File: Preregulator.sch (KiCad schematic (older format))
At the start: 26 parts, among them Q1 3904, Q2 3904, Q3 4403, Q4 4403, Q5 AO4805

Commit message: First working version
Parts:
- added C48: 100n, IPC7351-Nominal:CAPC1608X55, symbol C-0603
- added C55: 470u, pth-passive:C-ALUM-10mm, symbol C-ALUM-10mm
- added TP5: PREREG, conn-test:TEST-SMD-SMALL, symbol TESTPOINT
- L1: footprint manuf:BOURNS-SRN5040 -> (none); BOM (none) -> DIST DIGIKEY M8921-ND
- R17: value 20k -> 22k; BOM RES SMD 20k 1% [0603] -> RES SMD 22k 1% [0603]
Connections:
- net labels added: GND, PWR
- net labels removed: PWRGND
- wire segments 61 -> 67
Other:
- note added: "-0.5V"
- note added: "0V"
- note added: "3.3V"
- note added: "Vin"
- note added: "Vin-0.7V"
- note added: "Vin-13.9V"
- note added: "Vin-14.6V"
- note removed: "M8921-ND"
- moved on the sheet: C1, C2, C24, C25, C26, C3, C4, C41, C5, C6, D1, L1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

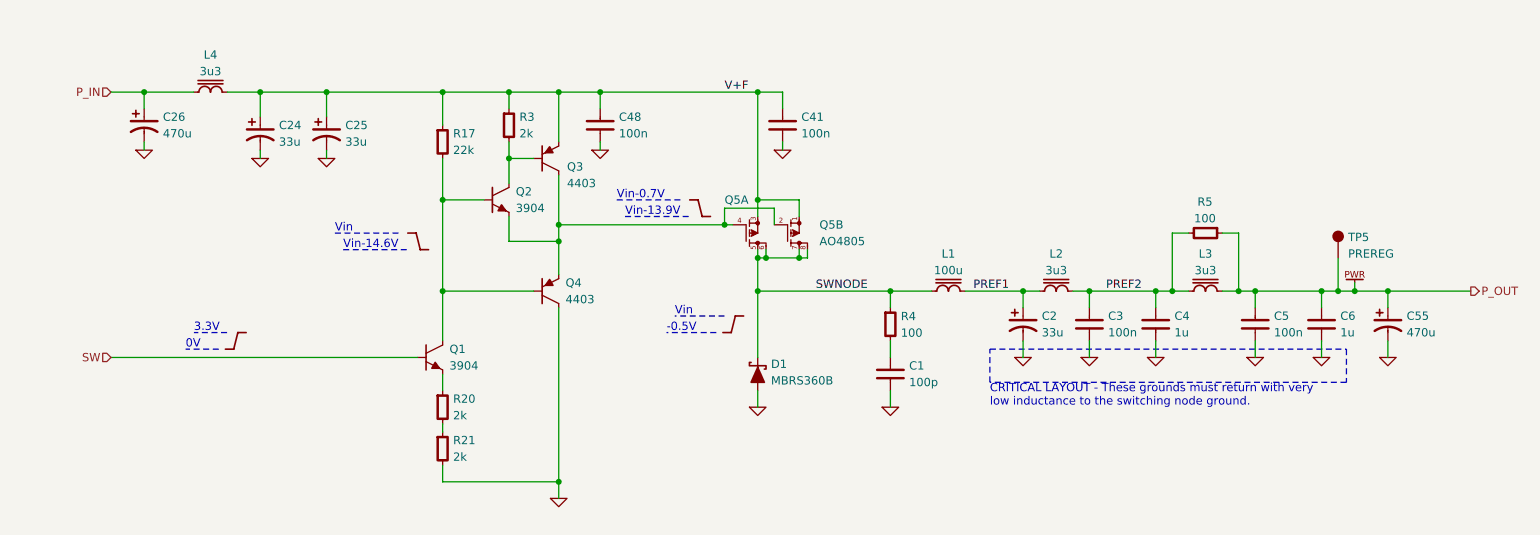
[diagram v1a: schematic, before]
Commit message: Reannotate component references
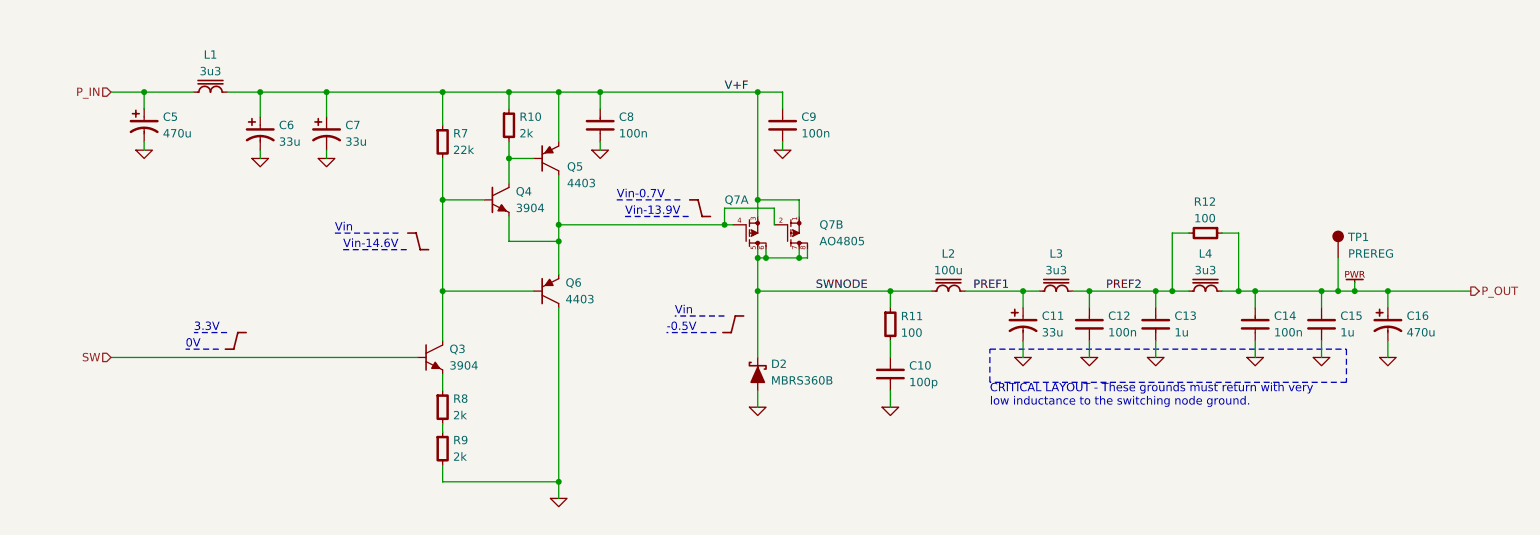
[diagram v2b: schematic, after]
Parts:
- renumbered C1 to C10, C2 to C11, C3 to C12, C4 to C13, C5 to C14, C6 to C15, C55 to C16, C26 to C5, C24 to C6, C25 to C7, C48 to C8, C41 to C9, D1 to D2, L4 to L1, L1 to L2, L2 to L3, L3 to L4, Q1 to Q3, Q2 to Q4, Q3 to Q5, Q4 to Q6, Q5 to Q7, R3 to R10, R4 to R11, R5 to R12, R17 to R7, R20 to R8, R21 to R9, TP5 to TP1

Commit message: Piles and piles of work
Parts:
- removed C6, C7: 33u, IPC7351-Nominal:CAPAE660X570, symbol C-ALUM-660
- added C6: 470u, pth-passive:C-ALUM-10mm, symbol C-ALUM-10mm
- added C7: 6u8, IPC7351-Nominal:CAPC3216X70, symbol C-1206
- added TP14: SW, conn-test:TEST-SMD-SMALL, symbol TESTPOINT
- C10: value 100p -> 220p; BOM CAP MLCC 100pF C0G 50V 5% [0603] -> CAP MLCC 220p C0G 50V 10% [0603]
- C16, C5: BOM DIST DIGIKEY 1189-1280-ND -> DIST DIGIKEY 493-1868-ND
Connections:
- net GND: now also C6.2, C7.2
- net SW: now also TP14.1
- net V+F: now also C6.1, C7.1
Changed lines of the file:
@@
 P 6100 4600
 F 0 "C10" H 6213 4650 50  0000 L CNN
-F 1 "100p" H 6213 4550 50  0000 L CNN
+F 1 "220p" H 6213 4550 50  0000 L CNN
 F 2 "IPC7351-Nominal:CAPC1608X55" H 6100 4600 50  0001 C CNN
 F 3 "" H 6090 4575 60  0000 C CNN
-F 4 "Value" H 6100 4600 60  0001 C CNN "Manuf"
-F 5 "CAP MLCC 100pF C0G 50V 5% [0603]" H 6900 5150 60  0001 C CNN "BOM"
+F 4 "CAP MLCC 220p C0G 50V 10% [0603]" H 6900 5150 60  0001 C CNN "BOM"
+F 5 "Value" H 6100 4600 60  0001 C CNN "Manuf"
 	1    6100 4600
 	1    0    0    -1
@@
 Text Label 7400 4100 0    50   ~ 0
 PREF2
-$Comp
-L C-ALUM-660 C7
-U 1 1 55CD0145
-P 2700 3150
-F 0 "C7" H 2813 3200 50  0000 L CNN
-F 1 "33u" H 2813 3100 50  0000 L CNN
-F 2 "IPC7351-Nominal:CAPAE660X570" H 2700 3150 50  0001 C CNN
-F 3 "" H 2690 3125 60  0000 C CNN
-F 4 "DIST DIGIKEY P15444CT-ND" H 2700 3150 60  0001 C CNN "BOM"
-	1    2700 3150
-	1    0    0    -1
-$EndComp
 Wire Wire Line
 	2700 3050 2700 2900
 Connection ~ 2700 2900
-$Comp
-L C-ALUM-660 C6
-U 1 1 55CD0271
-P 2300 3150
-F 0 "C6" H 2413 3200 50  0000 L CNN
-F 1 "33u" H 2413 3100 50  0000 L CNN
-F 2 "IPC7351-Nominal:CAPAE660X570" H 2300 3150 50  0001 C CNN
-F 3 "" H 2290 3125 60  0000 C CNN
-F 4 "DIST DIGIKEY P15444CT-ND" H 2300 3150 60  0001 C CNN "BOM"
-	1    2300 3150
-	1    0    0    -1
-$EndComp
 Wire Wire Line
 	2300 3050 2300 2900
@@
 F 2 "pth-passive:C-ALUM-10mm" H 1600 3100 50  0001 C CNN
 F 3 "" H 1590 3075 60  0000 C CNN
-F 4 "DIST DIGIKEY 1189-1280-ND" H 1600 3100 60  0001 C CNN "BOM"
+F 4 "DIST DIGIKEY 493-1868-ND" H 1600 3100 60  0001 C CNN "BOM"
 	1    1600 3100
 	1    0    0    -1
@@
 	5450 3250 5450 3200
 $Comp
-L GND #PWR22
+L GND #PWR21
 U 1 1 55D3B7DF
 P 5300 4800
-F 0 "#PWR22" H 5300 4800 30  0001 C CNN
+F 0 "#PWR21" H 5300 4800 30  0001 C CNN
 F 1 "GND" H 5300 4730 30  0001 C CNN
 F 2 "" H 5300 4800 60  0000 C CNN
@@
 $EndComp
 $Comp
-L GND #PWR24
+L GND #PWR23
 U 1 1 55D3B842
 P 6100 4800
-F 0 "#PWR24" H 6100 4800 30  0001 C CNN
+F 0 "#PWR23" H 6100 4800 30  0001 C CNN
 F 1 "GND" H 6100 4730 30  0001 C CNN
 F 2 "" H 6100 4800 60  0000 C CNN
@@
 $EndComp
 $Comp
-L GND #PWR25
+L GND #PWR24
 U 1 1 55D3B89E
 P 6900 4500
-F 0 "#PWR25" H 6900 4500 30  0001 C CNN
+F 0 "#PWR24" H 6900 4500 30  0001 C CNN
 F 1 "GND" H 6900 4430 30  0001 C CNN
 F 2 "" H 6900 4500 60  0000 C CNN
@@
 $EndComp
 $Comp
-L GND #PWR26
+L GND #PWR25
 U 1 1 55D3B8FA
 P 7300 4500
-F 0 "#PWR26" H 7300 4500 30  0001 C CNN
+F 0 "#PWR25" H 7300 4500 30  0001 C CNN
 F 1 "GND" H 7300 4430 30  0001 C CNN
 F 2 "" H 7300 4500 60  0000 C CNN
@@
 $EndComp
 $Comp
-L GND #PWR27
+L GND #PWR26
 U 1 1 55D3B956
 P 7700 4500
-F 0 "#PWR27" H 7700 4500 30  0001 C CNN
+F 0 "#PWR26" H 7700 4500 30  0001 C CNN
 F 1 "GND" H 7700 4430 30  0001 C CNN
 F 2 "" H 7700 4500 60  0000 C CNN
@@
 $EndComp
 $Comp
-L GND #PWR28
+L GND #PWR27
 U 1 1 55D3B9B2
 P 8300 4500
-F 0 "#PWR28" H 8300 4500 30  0001 C CNN
+F 0 "#PWR27" H 8300 4500 30  0001 C CNN
 F 1 "GND" H 8300 4430 30  0001 C CNN
 F 2 "" H 8300 4500 60  0000 C CNN
@@
 $EndComp
 $Comp
-L GND #PWR29
+L GND #PWR28
 U 1 1 55D3BA0E
 P 8700 4500
-F 0 "#PWR29" H 8700 4500 30  0001 C CNN
+F 0 "#PWR28" H 8700 4500 30  0001 C CNN
 F 1 "GND" H 8700 4430 30  0001 C CNN
 F 2 "" H 8700 4500 60  0000 C CNN
@@
 $EndComp
 $Comp
-L GND #PWR20
+L GND #PWR19
 U 1 1 55D3BB43
 P 4100 5350
-F 0 "#PWR20" H 4100 5350 30  0001 C CNN
+F 0 "#PWR19" H 4100 5350 30  0001 C CNN
 F 1 "GND" H 4100 5280 30  0001 C CNN
 F 2 "" H 4100 5350 60  0000 C CNN
@@
 $EndComp
 $Comp
-L GND #PWR19
+L GND #PWR18
 U 1 1 55D3BD37
 P 2700 3300
-F 0 "#PWR19" H 2700 3300 30  0001 C CNN
+F 0 "#PWR18" H 2700 3300 30  0001 C CNN
 F 1 "GND" H 2700 3230 30  0001 C CNN
 F 2 "" H 2700 3300 60  0000 C CNN
@@
 $EndComp
 $Comp
-L GND #PWR18
+L GND #PWR17
 U 1 1 55D3BD93
 P 2300 3300
-F 0 "#PWR18" H 2300 3300 30  0001 C CNN
+F 0 "#PWR17" H 2300 3300 30  0001 C CNN
 F 1 "GND" H 2300 3230 30  0001 C CNN
 F 2 "" H 2300 3300 60  0000 C CNN
@@
 $EndComp
 $Comp
-L GND #PWR17
+L GND #PWR16
 U 1 1 55D3BDEF
 P 1600 3250
-F 0 "#PWR17" H 1600 3250 30  0001 C CNN
+F 0 "#PWR16" H 1600 3250 30  0001 C CNN
 F 1 "GND" H 1600 3180 30  0001 C CNN
 F 2 "" H 1600 3250 60  0000 C CNN
@@
 $EndComp
 $Comp
-L GND #PWR23
+L GND #PWR22
 U 1 1 55D3BE67
 P 5450 3250
-F 0 "#PWR23" H 5450 3250 30  0001 C CNN
+F 0 "#PWR22" H 5450 3250 30  0001 C CNN
 F 1 "GND" H 5450 3180 30  0001 C CNN
 F 2 "" H 5450 3250 60  0000 C CNN
@@
 Connection ~ 4350 2900
 $Comp
-L GND #PWR21
+L GND #PWR20
 U 1 1 55D41998
 P 4350 3250
-F 0 "#PWR21" H 4350 3250 30  0001 C CNN
+F 0 "#PWR20" H 4350 3250 30  0001 C CNN
 F 1 "GND" H 4350 3180 30  0001 C CNN
 F 2 "" H 4350 3250 60  0000 C CNN
@@
 Connection ~ 8800 4100
 $Comp
-L PWR #PWR30
+L PWR #PWR29
 U 1 1 55D49638
 P 8900 4050
-F 0 "#PWR30" H 8900 4050 50  0001 C CNN
+F 0 "#PWR29" H 8900 4050 50  0001 C CNN
 F 1 "PWR" H 8900 4050 50  0001 C CNN
 F 2 "" H 8900 4050 60  0000 C CNN
@@
 	8900 4050 8900 4100
 Connection ~ 8900 4100
-$Comp
-L STEP #SYM1
-U 1 1 55D506A0
-P 2150 4400
-F 0 "#SYM1" H 2150 4400 60  0001 C CNN
-F 1 "STEP" H 2140 4400 60  0001 C CNN
-F 2 "" H 2140 4400 60  0000 C CNN
-F 3 "" H 2140 4400 60  0000 C CNN
-	1    2150 4400
-	1    0    0    -1
-$EndComp
 Wire Notes Line
 	2050 4450 1850 4450
@@
 Text Notes 1900 4350 0    50   ~ 0
 3.3V
-$Comp
-L STEP #SYM2
-U 1 1 55D50AAE
-P 3250 3800
-F 0 "#SYM2" H 3250 3800 60  0001 C CNN
-F 1 "STEP" H 3240 3800 60  0001 C CNN
-F 2 "" H 3240 3800 60  0000 C CNN
-F 3 "" H 3240 3800 60  0000 C CNN
-	1    3250 3800
-	1    0    0    1
-$EndComp
-Text Notes 2750 3750 0    50   ~ 0
+Text Notes 2600 3750 0    50   ~ 0
 Vin
-Text Notes 2800 3850 0    50   ~ 0
+Text Notes 2650 3850 0    50   ~ 0
 Vin-14.6V
 Wire Notes Line
-	2750 3750 3150 3750
-Wire Notes Line
-	2800 3850 3200 3850
-$Comp
-L STEP #SYM3
-U 1 1 55D527C7
-P 4950 3600
-F 0 "#SYM3" H 4950 3600 60  0001 C CNN
-F 1 "STEP" H 4940 3600 60  0001 C CNN
-F 2 "" H 4940 3600 60  0000 C CNN
-F 3 "" H 4940 3600 60  0000 C CNN
-	1    4950 3600
-	1    0    0    1
-$EndComp
-Text Notes 4450 3550 0    50   ~ 0
+	2600 3750 3000 3750
+Wire Notes Line
+	2650 3850 3050 3850
+Text Notes 4350 3550 0    50   ~ 0
 Vin-0.7V
-Text Notes 4500 3650 0    50   ~ 0
+Text Notes 4400 3650 0    50   ~ 0
 Vin-13.9V
 Wire Notes Line
-	4450 3550 4850 3550
-Wire Notes Line
-	4500 3650 4900 3650
-$Comp
-L STEP #SYM4
-U 1 1 55D5289E
-P 5150 4300
-F 0 "#SYM4" H 5150 4300 60  0001 C CNN
-F 1 "STEP" H 5140 4300 60  0001 C CNN
-F 2 "" H 5140 4300 60  0000 C CNN
-F 3 "" H 5140 4300 60  0000 C CNN
-	1    5150 4300
-	1    0    0    -1
-$EndComp
-Wire Notes Line
-	5050 4350 4750 4350
-Wire Notes Line
-	5100 4250 4800 4250
-Text Notes 4750 4350 0    50   ~ 0
+	4350 3550 4750 3550
+Wire Notes Line
+	4400 3650 4800 3650
+Wire Notes Line
+	4900 4350 4600 4350
+Wire Notes Line
+	4950 4250 4650 4250
+Text Notes 4600 4350 0    50   ~ 0
 -0.5V
-Text Notes 4800 4250 0    50   ~ 0
+Text Notes 4650 4250 0    50   ~ 0
 Vin
 $Comp
@@
 F 2 "pth-passive:C-ALUM-10mm" H 9100 4300 50  0001 C CNN
 F 3 "" H 9090 4275 60  0000 C CNN
-F 4 "DIST DIGIKEY 1189-1280-ND" H 9100 4300 60  0001 C CNN "BOM"
+F 4 "DIST DIGIKEY 493-1868-ND" H 9100 4300 60  0001 C CNN "BOM"
 	1    9100 4300
 	1    0    0    -1
@@
 Connection ~ 9100 4100
 $Comp
-L GND #PWR31
+L GND #PWR30
 U 1 1 55D4D0A0
 P 9100 4500
-F 0 "#PWR31" H 9100 4500 30  0001 C CNN
+F 0 "#PWR30" H 9100 4500 30  0001 C CNN
 F 1 "GND" H 9100 4430 30  0001 C CNN
 F 2 "" H 9100 4500 60  0000 C CNN
@@
 Wire Wire Line
 	9100 4500 9100 4400
+$Comp
+L C-ALUM-10mm C6
+U 1 1 55DBA4ED
+P 2300 3150
+F 0 "C6" H 2413 3200 50  0000 L CNN
+F 1 "470u" H 2413 3100 50  0000 L CNN
+F 2 "pth-passive:C-ALUM-10mm" H 2300 3150 50  0001 C CNN
+F 3 "" H 2290 3125 60  0000 C CNN
+F 4 "DIST DIGIKEY 493-1868-ND" H 2300 3150 60  0001 C CNN "BOM"
+	1    2300 3150
+	1    0    0    -1
+$EndComp
+$Comp
+L C-1206 C?
+U 1 1 55DC1E2B
+P 2700 3150
+AR Path="/55CEE1A2/55DC1E2B" Ref="C?"  Part="1"
+AR Path="/55C7F4BB/55DC1E2B" Ref="C7"  Part="1"
+F 0 "C7" H 2813 3200 50  0000 L CNN
+F 1 "6u8" H 2813 3100 50  0000 L CNN
+F 2 "IPC7351-Nominal:CAPC3216X70" H 2700 3150 50  0001 C CNN
+F 3 "" H 2690 3125 60  0000 C CNN
+F 4 "CAP MLCC 6u8 50V ≥X5R [1206]" H 3500 3700 60  0001 C CNN "BOM"
+F 5 "Value" H 2700 3150 60  0001 C CNN "Manuf"
+	1    2700 3150
+	1    0    0    -1
+$EndComp
+$Comp
+L TESTPOINT TP?
+U 1 1 55E0DF05
+P 2700 4400
+AR Path="/55C7FF09/55E0DF05" Ref="TP?"  Part="1"
+AR Path="/55C7F4BB/55E0DF05" Ref="TP14"  Part="1"
+F 0 "TP14" H 2760 4525 50  0000 L CNN
+F 1 "SW" H 2760 4425 50  0000 L CNN
+F 2 "conn-test:TEST-SMD-SMALL" H 2760 4375 50  0001 L CNN
+F 3 "" H 2700 4400 50  0000 C CNN
+	1    2700 4400
+	1    0    0    -1
+$EndComp
+Wire Wire Line
+	2700 4400 2700 4500
+Connection ~ 2700 4500
+$Comp
+L SQUARE #SYM1
+U 1 1 55E0EF64
+P 2250 4400
+F 0 "#SYM1" H 2250 4400 60  0001 C CNN
+F 1 "SQUARE" H 2250 4400 60  0001 C CNN
+F 2 "" H 2250 4400 60  0000 C CNN
+F 3 "" H 2250 4400 60  0000 C CNN
+	1    2250 4400
+	1    0    0    -1
+$EndComp
+$Comp
+L SQUARE #SYM2
+U 1 1 55E0F2E6
+P 3200 3800
+F 0 "#SYM2" H 3200 3800 60  0001 C CNN
+F 1 "SQUARE" H 3200 3800 60  0001 C CNN
+F 2 "" H 3200 3800 60  0000 C CNN
+F 3 "" H 3200 3800 60  0000 C CNN
+	1    3200 3800
+	1    0    0    1
+$EndComp
+$Comp
+L SQUARE #SYM3
+U 1 1 55E108F1
+P 4950 3600
+F 0 "#SYM3" H 4950 3600 60  0001 C CNN
+F 1 "SQUARE" H 4950 3600 60  0001 C CNN
+F 2 "" H 4950 3600 60  0000 C CNN
+F 3 "" H 4950 3600 60  0000 C CNN
+	1    4950 3600
+	1    0    0    1
+$EndComp
+$Comp
+L SQUARE #SYM4
+U 1 1 55E10D25
+P 5100 4300
+F 0 "#SYM4" H 5100 4300 60  0001 C CNN
+F 1 "SQUARE" H 5100 4300 60  0001 C CNN
+F 2 "" H 5100 4300 60  0000 C CNN
+F 3 "" H 5100 4300 60  0000 C CNN
+	1    5100 4300
+	1    0    0    -1
+$EndComp
 $EndSCHEMATC
